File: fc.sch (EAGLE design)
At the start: 66 parts, among them IC2 BN055, J2 USBC, U1 ATMEGA2560-16AU100A-M, U4 FT230XQ, U5 SI8621AB-B-IS, Y2 32.768kHz, Y3 16MHz

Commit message: Spannungsregler
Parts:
- added C13, C9: 22uF, SparkFun-Capacitors:22UF-0805-6.3V-20%
- added C14: 1nF, SparkFun-Capacitors:1.0NF/1000PF-0603-50V-10%
- added R5: 35.7k, SparkFun-Resistors:RESISTOR0603
- added R6: 11.5k, SparkFun-Resistors:RESISTOR0603
- added U3: LMZ21700, jonas_ti:LMZ21700
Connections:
- new net N$8: R5.1, R6.2, U3.FB
- new net N$9: C14.1, U3.SS
- net +3V3: now also C9.1, R5.2, U3.VOS, U3.VOUT
- net +5V: now also C13.1, U3.EN, U3.VIN
- net GND: now also C13.2, C14.2, C9.2, R6.1, U3.GND
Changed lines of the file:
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@@
 <layer number="145" name="DrillLegend_01-16" color="7" fill="1" visible="no" active="yes"/>
 <layer number="146" name="DrillLegend_01-20" color="7" fill="1" visible="no" active="yes"/>
+<layer number="148" name="Document_mirrored" color="7" fill="1" visible="no" active="no"/>
 <layer number="150" name="Notes" color="7" fill="1" visible="yes" active="yes"/>
 <layer number="151" name="HeatSink" color="7" fill="1" visible="yes" active="yes"/>
@@
 <layer number="154" name="FabDoc2" color="7" fill="1" visible="yes" active="yes"/>
 <layer number="155" name="FabDoc3" color="7" fill="1" visible="yes" active="yes"/>
+<layer number="156" name="gesam-Maß" color="1" fill="7" visible="no" active="no"/>
+<layer number="157" name="FaceMchng" color="3" fill="1" visible="no" active="no"/>
+<layer number="158" name="FaceMMeas" color="3" fill="1" visible="no" active="no"/>
+<layer number="159" name="Geh-Bear2" color="1" fill="7" visible="no" active="no"/>
+<layer number="160" name="Topologie" color="9" fill="1" visible="no" active="no"/>
+<layer number="161" name="tomplace2" color="7" fill="1" visible="no" active="no"/>
 <layer number="199" name="Contour" color="7" fill="1" visible="yes" active="yes"/>
 <layer number="200" name="scaled_image_import" color="1" fill="10" visible="yes" active="yes"/>
@@
 <layer number="250" name="Descript" color="3" fill="1" visible="no" active="no"/>
 <layer number="251" name="SMDround" color="12" fill="11" visible="no" active="no"/>
+<layer number="252" name="BR-BS" color="7" fill="1" visible="no" active="no"/>
+<layer number="253" name="BR-LS" color="7" fill="1" visible="no" active="no"/>
 <layer number="254" name="cooling" color="7" fill="1" visible="yes" active="yes"/>
 <layer number="255" name="routoute" color="7" fill="1" visible="yes" active="yes"/>
@@
 <part name="GND1" library="supply1" library_urn="urn:adsk.eagle:library:371" deviceset="GND" device=""/>
 <part name="+3V6" library="supply1" library_urn="urn:adsk.eagle:library:371" deviceset="+3V3" device=""/>
+<part name="FRAME5" library="frames" library_urn="urn:adsk.eagle:library:229" deviceset="A3L-LOC" device=""/>
+<part name="U3" library="jonas_ti" library_urn="urn:adsk.eagle:library:539711" deviceset="LMZ21700" device=""/>
+<part name="GND3" library="supply1" library_urn="urn:adsk.eagle:library:371" deviceset="GND" device=""/>
+<part name="C9" library="SparkFun-Capacitors" library_urn="urn:adsk.eagle:library:510" deviceset="22UF" device="-0805-6.3V-20%" package3d_urn="urn:adsk.eagle:package:37429/1" value="22uF"/>
+<part name="R5" library="SparkFun-Resistors" library_urn="urn:adsk.eagle:library:532" deviceset="RESISTOR" device="0603" package3d_urn="urn:adsk.eagle:package:39650/1" value="35.7k"/>
+<part name="R6" library="SparkFun-Resistors" library_urn="urn:adsk.eagle:library:532" deviceset="RESISTOR" device="0603" package3d_urn="urn:adsk.eagle:package:39650/1" value="11.5k"/>
+<part name="C13" library="SparkFun-Capacitors" library_urn="urn:adsk.eagle:library:510" deviceset="22UF" device="-0805-6.3V-20%" package3d_urn="urn:adsk.eagle:package:37429/1" value="22uF"/>
+<part name="C14" library="SparkFun-Capacitors" library_urn="urn:adsk.eagle:library:510" deviceset="1.0NF/1000PF" device="-0603-50V-10%" package3d_urn="urn:adsk.eagle:package:37414/1" value="1nF"/>
+<part name="P+2" library="supply1" library_urn="urn:adsk.eagle:library:371" deviceset="+5V" device=""/>
+<part name="+3V9" library="supply1" library_urn="urn:adsk.eagle:library:371" deviceset="+3V3" device=""/>
 </parts>
 <sheets>
@@
 </segment>
 </net>
+</nets>
+</sheet>
+<sheet>
+<description>5V-3V3 Regler</description>
+<plain>
+</plain>
+<instances>
+<instance part="FRAME5" gate="G$1" x="0" y="0" smashed="yes">
+<attribute name="DRAWING_NAME" x="344.17" y="15.24" size="2.54" layer="94"/>
+<attribute name="LAST_DATE_TIME" x="344.17" y="10.16" size="2.286" layer="94"/>
+<attribute name="SHEET" x="357.505" y="5.08" size="2.54" layer="94"/>
+</instance>
+<instance part="U3" gate="G$1" x="68.58" y="205.74" smashed="yes">
+<attribute name="NAME" x="76.2" y="211.582" size="2.1844" layer="95"/>
+</instance>
+<instance part="GND3" gate="1" x="68.58" y="177.8" smashed="yes">
+<attribute name="VALUE" x="66.04" y="175.26" size="1.778" layer="96"/>
+</instance>
+<instance part="C9" gate="G$1" x="121.92" y="198.12" smashed="yes">
+<attribute name="NAME" x="123.444" y="201.041" size="1.778" layer="95"/>
+<attribute name="VALUE" x="123.444" y="195.961" size="1.778" layer="96"/>
+</instance>
+<instance part="R5" gate="G$1" x="109.22" y="198.12" smashed="yes">
+<attribute name="NAME" x="105.41" y="199.6186" size="1.778" layer="95"/>
+<attribute name="VALUE" x="105.41" y="194.818" size="1.778" layer="96"/>
+</instance>
+<instance part="R6" gate="G$1" x="101.6" y="190.5" smashed="yes" rot="R90">
+<attribute name="NAME" x="100.1014" y="186.69" size="1.778" layer="95" rot="R90"/>
+<attribute name="VALUE" x="104.902" y="186.69" size="1.778" layer="96" rot="R90"/>
+</instance>
+<instance part="C13" gate="G$1" x="48.26" y="198.12" smashed="yes">
+<attribute name="NAME" x="49.784" y="201.041" size="1.778" layer="95"/>
+<attribute name="VALUE" x="49.784" y="195.961" size="1.778" layer="96"/>
+</instance>
+<instance part="C14" gate="G$1" x="60.96" y="193.04" smashed="yes">
+<attribute name="NAME" x="62.484" y="195.961" size="1.778" layer="95"/>
+<attribute name="VALUE" x="62.484" y="190.881" size="1.778" layer="96"/>
+</instance>
+<instance part="P+2" gate="1" x="48.26" y="210.82" smashed="yes">
+<attribute name="VALUE" x="45.72" y="205.74" size="1.778" layer="96" rot="R90"/>
+</instance>
+<instance part="+3V9" gate="G$1" x="129.54" y="205.74" smashed="yes" rot="R270">
+<attribute name="VALUE" x="124.46" y="208.28" size="1.778" layer="96"/>
+</instance>
+</instances>
+<busses>
+</busses>
+<nets>
+<net name="GND" class="0">
+<segment>
+<pinref part="U3" gate="G$1" pin="GND"/>
+<wire x1="71.12" y1="198.12" x2="68.58" y2="198.12" width="0.1524" layer="91"/>
+<pinref part="GND3" gate="1" pin="GND"/>
+<wire x1="68.58" y1="198.12" x2="68.58" y2="182.88" width="0.1524" layer="91"/>
+<pinref part="R6" gate="G$1" pin="1"/>
+<wire x1="68.58" y1="182.88" x2="68.58" y2="180.34" width="0.1524" layer="91"/>
+<wire x1="101.6" y1="185.42" x2="101.6" y2="182.88" width="0.1524" layer="91"/>
+<pinref part="C9" gate="G$1" pin="2"/>
+<wire x1="121.92" y1="195.58" x2="121.92" y2="182.88" width="0.1524" layer="91"/>
+<wire x1="101.6" y1="182.88" x2="121.92" y2="182.88" width="0.1524" layer="91"/>
+<wire x1="101.6" y1="182.88" x2="68.58" y2="182.88" width="0.1524" layer="91"/>
+<junction x="101.6" y="182.88"/>
+<junction x="68.58" y="182.88"/>
+<pinref part="C14" gate="G$1" pin="2"/>
+<wire x1="60.96" y1="190.5" x2="60.96" y2="182.88" width="0.1524" layer="91"/>
+<wire x1="60.96" y1="182.88" x2="68.58" y2="182.88" width="0.1524" layer="91"/>
+<pinref part="C13" gate="G$1" pin="2"/>
+<wire x1="48.26" y1="195.58" x2="48.26" y2="182.88" width="0.1524" layer="91"/>
+<wire x1="48.26" y1="182.88" x2="60.96" y2="182.88" width="0.1524" layer="91"/>
+<junction x="60.96" y="182.88"/>
+</segment>
+</net>
+<net name="N$8" class="0">
+<segment>
+<pinref part="R6" gate="G$1" pin="2"/>
+<pinref part="R5" gate="G$1" pin="1"/>
+<pinref part="U3" gate="G$1" pin="FB"/>
+<wire x1="99.06" y1="198.12" x2="101.6" y2="198.12" width="0.1524" layer="91"/>
+<wire x1="101.6" y1="198.12" x2="101.6" y2="195.58" width="0.1524" layer="91"/>
+<wire x1="104.14" y1="198.12" x2="101.6" y2="198.12" width="0.1524" layer="91"/>
+<junction x="101.6" y="198.12"/>
+</segment>
+</net>
+<net name="N$9" class="0">
+<segment>
+<pinref part="C14" gate="G$1" pin="1"/>
+<wire x1="60.96" y1="198.12" x2="60.96" y2="200.66" width="0.1524" layer="91"/>
+<pinref part="U3" gate="G$1" pin="SS"/>
+<wire x1="60.96" y1="200.66" x2="71.12" y2="200.66" width="0.1524" layer="91"/>
+</segment>
+</net>
+<net name="+5V" class="0">
+<segment>
+<wire x1="48.26" y1="203.2" x2="48.26" y2="205.74" width="0.1524" layer="91"/>
+<pinref part="C13" gate="G$1" pin="1"/>
+<pinref part="U3" gate="G$1" pin="VIN"/>
+<wire x1="48.26" y1="205.74" x2="48.26" y2="208.28" width="0.1524" layer="91"/>
+<wire x1="71.12" y1="205.74" x2="68.58" y2="205.74" width="0.1524" layer="91"/>
+<pinref part="U3" gate="G$1" pin="EN"/>
+<wire x1="71.12" y1="203.2" x2="68.58" y2="203.2" width="0.1524" layer="91"/>
+<wire x1="68.58" y1="203.2" x2="68.58" y2="205.74" width="0.1524" layer="91"/>
+<wire x1="68.58" y1="205.74" x2="48.26" y2="205.74" width="0.1524" layer="91"/>
+<junction x="68.58" y="205.74"/>
+<junction x="48.26" y="205.74"/>
+<pinref part="P+2" gate="1" pin="+5V"/>
+</segment>
+</net>
+<net name="+3V3" class="0">
+<segment>
+<pinref part="U3" gate="G$1" pin="VOS"/>
+<wire x1="99.06" y1="200.66" x2="116.84" y2="200.66" width="0.1524" layer="91"/>
+<wire x1="116.84" y1="200.66" x2="116.84" y2="198.12" width="0.1524" layer="91"/>
+<pinref part="R5" gate="G$1" pin="2"/>
+<wire x1="116.84" y1="198.12" x2="114.3" y2="198.12" width="0.1524" layer="91"/>
+<wire x1="116.84" y1="200.66" x2="116.84" y2="205.74" width="0.1524" layer="91"/>
+<junction x="116.84" y="200.66"/>
+<pinref part="U3" gate="G$1" pin="VOUT"/>
+<wire x1="116.84" y1="205.74" x2="99.06" y2="205.74" width="0.1524" layer="91"/>
+<junction x="116.84" y="205.74"/>
+<pinref part="C9" gate="G$1" pin="1"/>
+<wire x1="116.84" y1="205.74" x2="121.92" y2="205.74" width="0.1524" layer="91"/>
+<wire x1="121.92" y1="205.74" x2="121.92" y2="203.2" width="0.1524" layer="91"/>
+<wire x1="121.92" y1="205.74" x2="127" y2="205.74" width="0.1524" layer="91"/>
+<junction x="121.92" y="205.74"/>
+<pinref part="+3V9" gate="G$1" pin="+3V3"/>
+</segment>
+</net>

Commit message: FTDI hauptsächlich
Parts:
- removed C24, C25: 100nF, rcl:C-EUC0603
- removed LED0: (no value), led:LEDCHIP-LED0603
- removed PPM0: (no value), pinhead:PINHD-1X3
- removed R20, R21: 27, rcl:R-EU_R0603
- removed R22, R23: 4k7, rcl:R-EU_R0603
- removed U5: SI8621AB-B-IS, SI8621AB-B-IS:SI8621AB-B-IS
- added C7, C8: 100n, resistor:C-EUC0603
- added LED8: (no value), led:LEDCHIP-LED0603
- added PPM8: (no value), pinhead:PINHD-1X3
- added R13: 100, rcl:R-EU_R0603
- added R4: 10k, resistor:R-EU_R0603
- added R7: 4.7k, SparkFun-Resistors:4.7KOHM-0603-1/10W-1%
- added R8: 270, SparkFun-Resistors:RESISTOR0603
- added U2: ATMEGA2560-16AU100A-M, ATMEGA2560:ATMEGA2560-16AU100A-M
- C1: value 100n -> 22uF; device resistor:C-EUC0603 -> SparkFun-Capacitors:22UF-0805-6.3V-20%
- C10: value 47pF -> 8pF
- C11: value 47pF -> 120n; device rcl:C-EUC0603 -> resistor:C-EUC0603
- C12: value 10nF -> 100nF
- C13: value 22uF -> 6.8n; device SparkFun-Capacitors:22UF-0805-6.3V-20% -> resistor:C-EUC0603
- C14: value 1nF -> 0.1uF; device SparkFun-Capacitors:1.0NF/1000PF-0603-50V-10% -> SparkFun-Capacitors:0.1UF-0603-25V-5%
- C16: value 100nF -> 22p; device rcl:C-EUC0603 -> resistor:C-EUC0603
- C17: value 4.7µF -> 22p; device Kondensatoren (rev17a):WCAP-ASLI_4X5,5_865080640004 -> resistor:C-EUC0603
- C18: value 22p -> 47pF; device resistor:C-EUC0603 -> SparkFun-Capacitors:47PF-0603-50V-5%
- C19: value 8pF -> 47pF; device rcl:C-EUC0603 -> SparkFun-Capacitors:47PF-0603-50V-5%
- C2: value 6.8n -> 22uF; device resistor:C-EUC0603 -> SparkFun-Capacitors:22UF-0805-6.3V-20%
- C20: value 8pF -> 0.1uF; device rcl:C-EUC0603 -> SparkFun-Capacitors:0.1UF-0603-25V-5%
- C21: value 100nF -> 10nF; device rcl:C-EUC0603 -> SparkFun-Capacitors:10NF-0603-50V-10%
- C22: value 100nF -> 4.7uF; device rcl:C-EUC0603 -> SparkFun-Capacitors:4.7UF0603
- C3: value 120n -> 1nF; device resistor:C-EUC0603 -> SparkFun-Capacitors:1.0NF/1000PF-0603-50V-10%
- C4: value 100n -> 8pF; device resistor:C-EUC0603 -> rcl:C-EUC0603
- C5: value 22p -> 100nF; device resistor:C-EUC0603 -> rcl:C-EUC0603
- C9: value 22uF -> 100nF; device SparkFun-Capacitors:22UF-0805-6.3V-20% -> rcl:C-EUC0603
- LED_RX1, LED_TX1: device led:LEDCHIP-LED0603 -> SparkFun-LED:LED0603
- R1: value 10k -> 35.7k; device resistor:R-EU_R0603 -> SparkFun-Resistors:RESISTOR0603
- R10: value 100 -> 27; device rcl:R-EU_R0603 -> SparkFun-Resistors:27OHM-0603-1/10W-1%
- R14: value 270 -> 100
- R19: value 100 -> (none); device rcl:R-EU_R0603 -> resistor:R-EU_R0603
- R2: value (none) -> 11.5k; device resistor:R-EU_R0603 -> SparkFun-Resistors:RESISTOR0603
- R5: value 35.7k -> 270
- R6: value 11.5k -> 4.7k; device SparkFun-Resistors:RESISTOR0603 -> SparkFun-Resistors:4.7KOHM-0603-1/10W-1%
- R9: value 270 -> 27; device rcl:R-EU_R0603 -> SparkFun-Resistors:27OHM-0603-1/10W-1%
- U1: value ATMEGA2560-16AU100A-M -> LMZ21700; device ATMEGA2560:ATMEGA2560-16AU100A-M -> jonas_ti:LMZ21700
- U3: value LMZ21700 -> SI8621AB-B-IS; device jonas_ti:LMZ21700 -> SI8621AB-B-IS:SI8621AB-B-IS
- renumbered C23 to C6, IC2 to IC1, J2 to J1, R35 to R3, S2 to S1, Y3 to Y1
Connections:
- net !BNO_RST: now also U2A.(ICP1)_PD4; no longer U1A.(ICP1)_PD4
- net !RESET: now also U2A.!RESET; no longer U1A.!RESET
- net !SBUS: now also R19.1, U2A.(RXD2)_PH0; no longer R2.1, U1A.(RXD2)_PH0
- net +3V3: now also C11.1, C12.1, C13.1, C15.1, C5.1, C8.1, R19.2, R4.2, U1.VOS, U1.VOUT, U2B.AREF, U2B.AVCC, U2B.VCC, U2B.VCC_2, U2B.VCC_3, U2B.VCC_4, U3.VDD2; no longer C21.1, C22.1, C24.1, C25.1, C3.1, C4.1, R2.2, R5.2, U1B.AREF, U1B.AVCC, U1B.VCC, U1B.VCC_2, U1B.VCC_3, U1B.VCC_4, U3.VOS, U3.VOUT, U5.VDD2
- net +5V: now also C1.1, PPM8.2, U1.EN, U1.VIN; no longer C13.1, PPM0.2, U3.EN, U3.VIN
- net BNO_INT: now also U2A.(OC2A/PCINT4)_PB4; no longer U1A.(OC2A/PCINT4)_PB4
- net BNO_RX: now also U2A.(TXD1/INT3)_PD3; no longer U1A.(TXD1/INT3)_PD3
- net BNO_TX: now also U2A.(RXD1/INT2)_PD2; no longer U1A.(RXD1/INT2)_PD2
- net D+1: now also R10.2; no longer R20.2
- net D-1: now also R9.1; no longer R21.1
- net GND: now also C10.1, C11.2, C12.2, C15.2, C16.1, C17.1, C4.1, C5.2, C7.2, C8.2, LED8.C, PPM8.3, R2.1, U1.GND, U2B.GND, U2B.GND_2, U2B.GND_3, U2B.GND_4, U2B.GND_5, U3.GND2; no longer C14.2, C18.1, C19.1, C20.1, C21.2, C22.2, C24.2, C25.2, C4.2, C5.1, LED0.C, PPM0.3, R6.1, U1B.GND, U1B.GND_2, U1B.GND_3, U1B.GND_4, U1B.GND_5, U3.GND, U5.GND2
- net GNDIO: now also C14.2, C18.1, C19.1, C20.2, C21.2, C22.2, U3.GND1; no longer C10.1, C11.1, C12.2, C15.2, C16.2, C17.2, U5.GND1
- net LED0: now also R11.2, U2A.(ICP4)_PL0; no longer R15.2, U1A.(ICP4)_PL0
- net LED1: now also R12.2, U2A.(ICP5)_PL1; no longer R10.2, U1A.(ICP5)_PL1
- net LED2: now also R13.2, U2A.(T5)_PL2; no longer R11.2, U1A.(T5)_PL2
- net LED3: now also R14.2, U2A.(OC5A)_PL3; no longer R12.2, U1A.(OC5A)_PL3
- net LED4: now also R15.2, U2A.(OC5B)_PL4; no longer R16.2, U1A.(OC5B)_PL4
- net LED5: now also R16.2, U2A.(OC5C)_PL5; no longer R17.2, U1A.(OC5C)_PL5
- net LED6: now also R17.2, U2A.PL6; no longer R18.2, U1A.PL6
- net LED7: now also R18.2, U2A.PL7; no longer R19.2, U1A.PL7
- net MISO: now also U2A.(MISO/PCINT3)_PB3; no longer U1A.(MISO/PCINT3)_PB3
- net MOSI: now also U2A.MOSI/PCINT2)_PB2; no longer U1A.MOSI/PCINT2)_PB2
- net N$1: now also R4.1; no longer R1.1
- net N$12: now also C7.1; no longer C1.1
- net N$13: now also C17.2; no longer C5.2
- net N$15: now also LED2.A, R12.1; no longer LED1.A, R10.1
- net N$18: now also LED3.A, R13.1; no longer LED2.A, R11.1
- net N$2: now also R5.1; no longer R14.1
- net N$20: now also LED4.A, R14.1; no longer LED3.A, R12.1
- net N$22: now also LED5.A, R15.1; no longer LED4.A, R16.1
- net N$24: now also LED6.A, R16.1; no longer LED5.A, R17.1
- net N$25: now also C16.2; no longer C18.2
- net N$27: now also LED7.A, R17.1; no longer LED6.A, R18.1
- net N$29: now also LED8.A, R18.1; no longer LED7.A, R19.1
- net N$3: now also R8.2; no longer R9.2
- net N$31: now also LED1.A, R11.1; no longer LED0.A, R15.1
- net N$32: now also C10.2, U2A.XTAL1; no longer C19.2, U1A.XTAL1
- net N$33: now also C4.2, U2A.XTAL2; no longer C20.2, U1A.XTAL2
- net N$4: now also R5.2; no longer R14.2
- net N$5: now also R8.1; no longer R9.1
- net N$8: now also R1.1, R2.2, U1.FB; no longer R5.1, R6.2, U3.FB
- net N$9: now also C3.1, U1.SS; no longer C14.1, U3.SS
- net PPM0: now also PPM1.1, U2A.(OC1A/PCINT5)_PB5; no longer PPM0.1, U1A.(OC1A/PCINT5)_PB5
- net PPM1: now also PPM2.1, U2A.(OC1B/PCINT6)_PB6; no longer PPM1.1, U1A.(OC1B/PCINT6)_PB6
- net PPM2: now also PPM3.1, U2A.(OC0A/OC1C/PCINT7)_PB7; no longer PPM2.1, U1A.(OC0A/OC1C/PCINT7)_PB7
- net PPM3: now also PPM4.1, U2A.(OC3A/AIN1)_PE3; no longer PPM3.1, U1A.(OC3A/AIN1)_PE3
- net PPM4: now also PPM5.1, U2A.(OC3B/INT4)_PE4; no longer PPM4.1, U1A.(OC3B/INT4)_PE4
- net PPM5: now also PPM6.1, U2A.(OC3C/INT5)_PE5; no longer PPM5.1, U1A.(OC3C/INT5)_PE5
- net PPM6: now also PPM7.1, U2A.(OC4A)_PH3; no longer PPM6.1, U1A.(OC4A)_PH3
- net PPM7: now also PPM8.1, U2A.(OC4B)_PH4; no longer PPM7.1, U1A.(OC4B)_PH4
- net RXD: now also R7.1, U3.A2; no longer R23.1, U5.A2
- net SCK: now also U2A.(SCK/PCINT1)_PB1; no longer U1A.(SCK/PCINT1)_PB1
- net TXD: now also R6.1, U3.A1; no longer R22.1, U5.A1
- net USBDM1: now also C18.2, R9.2; no longer C11.2, R21.2
- net USBDP1: now also C19.2, R10.1; no longer C10.2, R20.1
- net USB_RX: now also U2A.(RXD0/PCINT8)_PE0, U3.B1; no longer U1A.(RXD0/PCINT8)_PE0, U5.B1
- net USB_TX: now also U2A.(TXD0)_PE1, U3.B2; no longer U1A.(TXD0)_PE1, U5.B2
- net VBUS: now also C20.1, C21.1, C22.1; no longer C12.1, C16.1, C17.1
- net VCCIO: now also C14.1, R6.2, R7.2, U3.VDD1; no longer C15.1, R22.2, R23.2, U5.VDD1

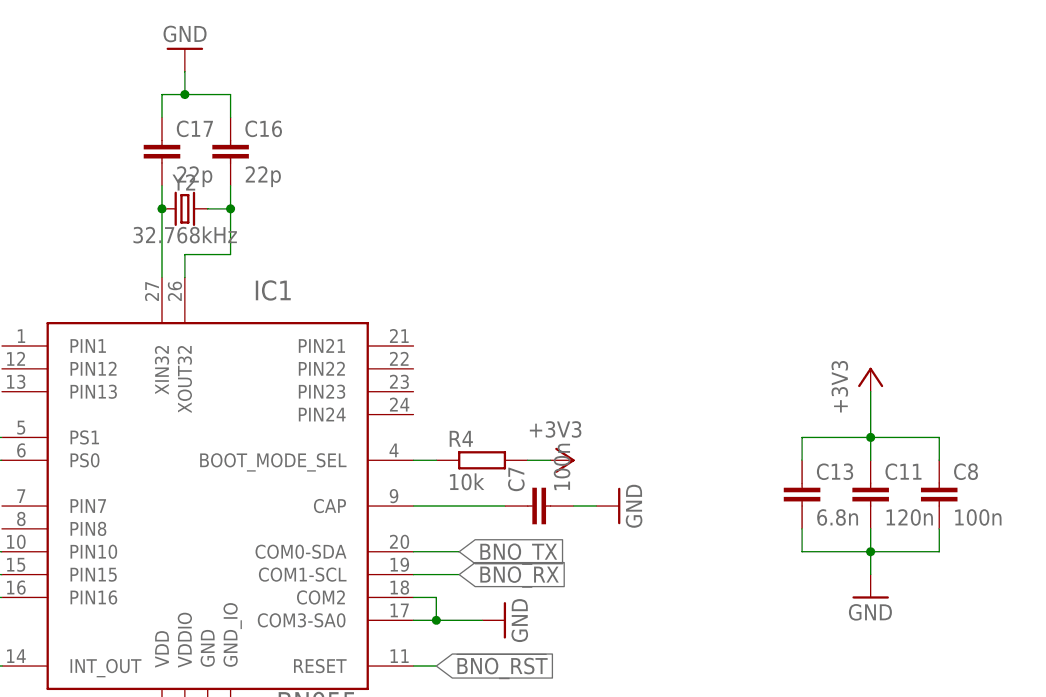
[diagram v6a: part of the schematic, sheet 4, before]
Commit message: changed caps to sparkfun lib
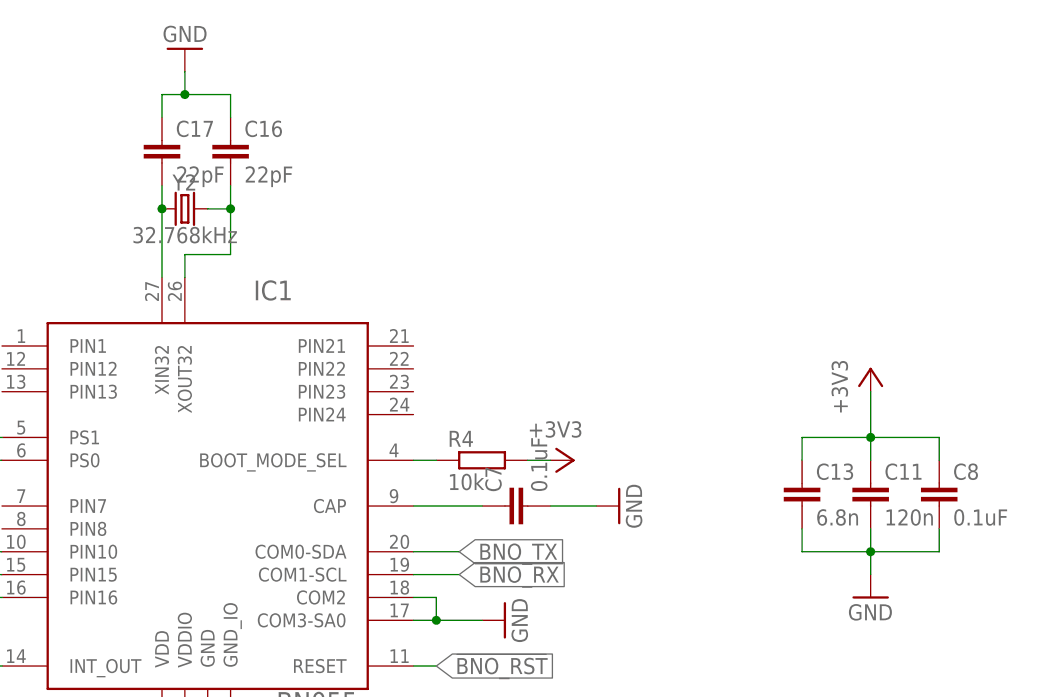
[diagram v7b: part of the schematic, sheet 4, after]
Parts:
- C10, C12, C15, C4, C5, C6, C9: device rcl:C-EUC0603 -> sparkfun-generic-cap:CAP_GENERIC0603
- C11, C13: device resistor:C-EUC0603 -> sparkfun-generic-cap:CAP_GENERIC0603
- C16, C17: value 22p -> 22pF; device resistor:C-EUC0603 -> SparkFun-Capacitors:22PF-0603-50V-5%
- C7, C8: value 100n -> 0.1uF; device resistor:C-EUC0603 -> SparkFun-Capacitors:0.1UF-0603-25V-(+80/-20%)
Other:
- moved on the sheet: C7
